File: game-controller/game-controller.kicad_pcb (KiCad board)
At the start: 2 copper layers, 3 parts, among them U1 STM32F103C8T6

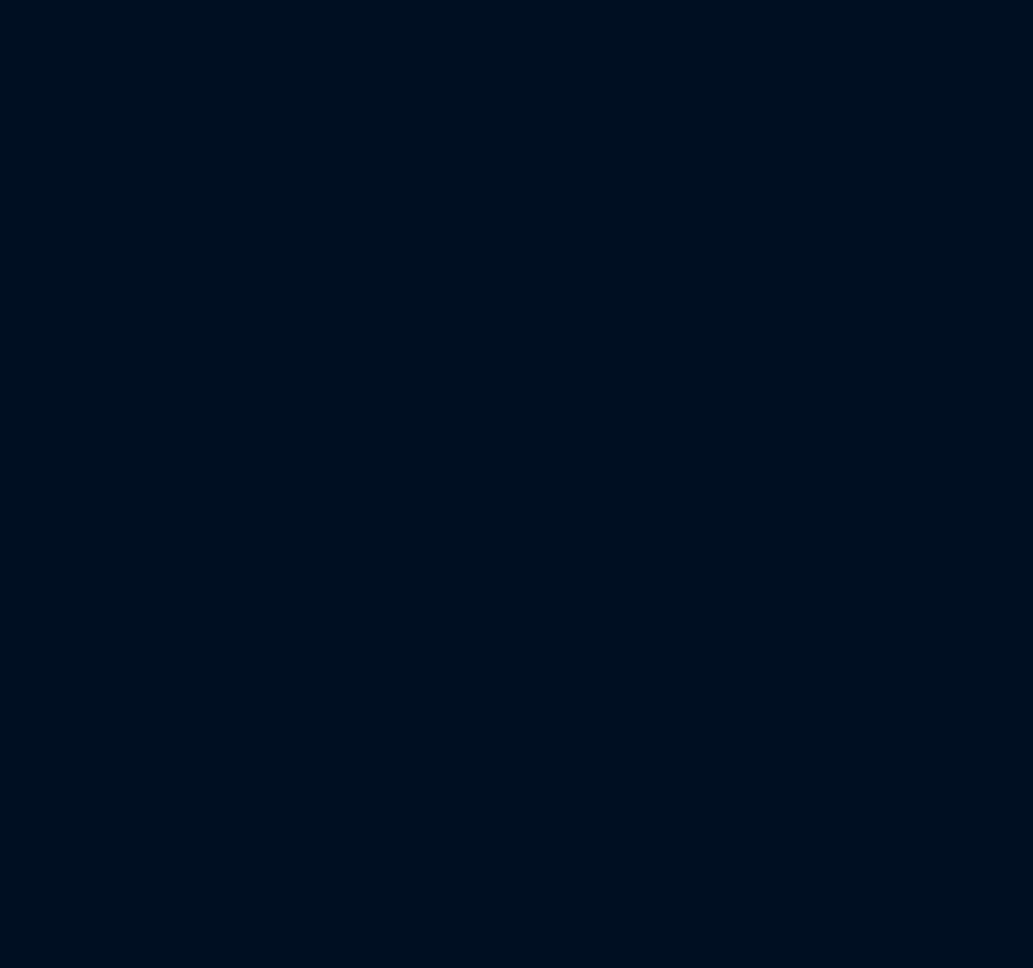
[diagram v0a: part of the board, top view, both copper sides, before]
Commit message: Added footprints
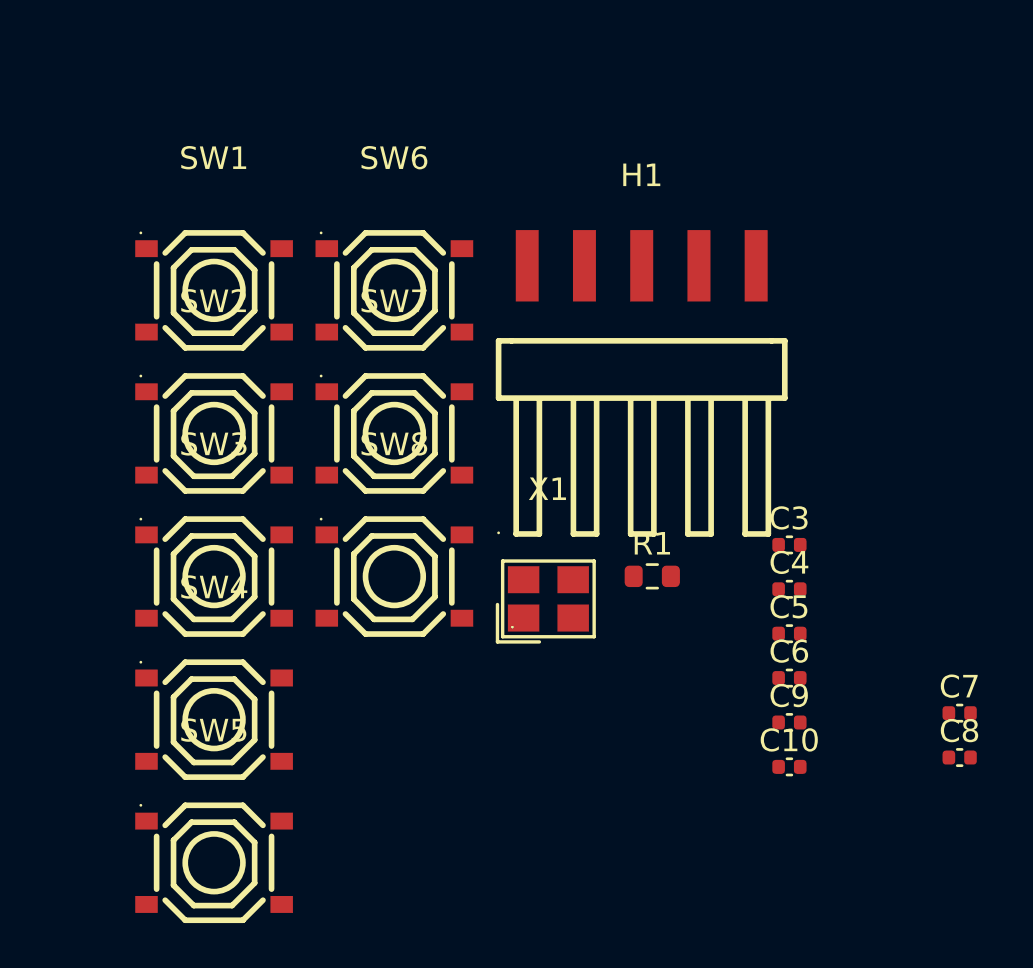
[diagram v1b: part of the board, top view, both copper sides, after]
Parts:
- added C10: 100nF/16V, Capacitor_SMD:C_0402_1005Metric, F.Cu at (208.9, 102.0)
- added C3: 100nF/16V, Capacitor_SMD:C_0402_1005Metric, F.Cu at (208.9, 92.1)
- added C4: 100nF/16V, Capacitor_SMD:C_0402_1005Metric, F.Cu at (208.9, 94.1)
- added C5: 10nF/50V, Capacitor_SMD:C_0402_1005Metric, F.Cu at (208.9, 96.1)
- added C6: 1uF/10V, Capacitor_SMD:C_0402_1005Metric, F.Cu at (208.9, 98.0)
- added C7: 20pF, Capacitor_SMD:C_0402_1005Metric, F.Cu at (216.4, 99.6)
- added C8: 20pF, Capacitor_SMD:C_0402_1005Metric, F.Cu at (216.4, 101.6)
- added C9: 100nF/16V, Capacitor_SMD:C_0402_1005Metric, F.Cu at (208.9, 100.0)
- added H1: HX PZ2.54-1X5P WT, parts:HDR-SMD_5P-P2.54-H-M-W12.8-N, F.Cu at (202.3, 79.8)
- added R1: 1.5kR, Resistor_SMD:R_0603_1608Metric, F.Cu at (202.8, 93.5)
- added SW1: TS-1187A-B-A-B, parts:SW-SMD_4P-L5.1-W5.1-P3.70-LS6.5-TL_H1.5, F.Cu at (183.3, 80.8)
- added SW2: TS-1187A-B-A-B, parts:SW-SMD_4P-L5.1-W5.1-P3.70-LS6.5-TL_H1.5, F.Cu at (183.3, 87.2)
- added SW3: TS-1187A-B-A-B, parts:SW-SMD_4P-L5.1-W5.1-P3.70-LS6.5-TL_H1.5, F.Cu at (183.3, 93.5)
- added SW4: TS-1187A-B-A-B, parts:SW-SMD_4P-L5.1-W5.1-P3.70-LS6.5-TL_H1.5, F.Cu at (183.3, 99.9)
- added SW5: TS-1187A-B-A-B, parts:SW-SMD_4P-L5.1-W5.1-P3.70-LS6.5-TL_H1.5, F.Cu at (183.3, 106.2)
- added SW6: TS-1187A-B-A-B, parts:SW-SMD_4P-L5.1-W5.1-P3.70-LS6.5-TL_H1.5, F.Cu at (191.3, 80.8)
- added SW7: TS-1187A-B-A-B, parts:SW-SMD_4P-L5.1-W5.1-P3.70-LS6.5-TL_H1.5, F.Cu at (191.3, 87.2)
- added SW8: TS-1187A-B-A-B, parts:SW-SMD_4P-L5.1-W5.1-P3.70-LS6.5-TL_H1.5, F.Cu at (191.3, 93.5)
- added X1: TAXM8M4RDBCCT2T, parts:CRYSTAL-SMD_4P-L3.2-W2.5-BL, F.Cu at (198.2, 94.5)
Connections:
- FPC1 pad 1: unconnected-(FPC1-VCC-Pad1) -> +3.3V
- FPC1 pad 2: unconnected-(FPC1-U/D-Pad2) -> /Y-1
- FPC1 pad 3: unconnected-(FPC1-BTN-Pad3) -> /BTN1
- FPC1 pad 4: unconnected-(FPC1-GND-Pad4) -> GND
- FPC1 pad 5: unconnected-(FPC1-L/R-Pad5) -> /X-1
- FPC2 pad 1: unconnected-(FPC2-VCC-Pad1) -> +3.3V
- FPC2 pad 2: unconnected-(FPC2-U/D-Pad2) -> /Y-2
- FPC2 pad 3: unconnected-(FPC2-BTN-Pad3) -> /BTN2
- FPC2 pad 4: unconnected-(FPC2-GND-Pad4) -> GND
- FPC2 pad 5: unconnected-(FPC2-L/R-Pad5) -> /X-2
- U1 pad 1: unconnected-(U1-VBAT-Pad1) -> +3.3V
- U1 pad 11: unconnected-(U1-PA1-Pad11) -> /Y-1
- U1 pad 12: unconnected-(U1-PA2-Pad12) -> /X-1
- U1 pad 13: unconnected-(U1-PA3-Pad13) -> /Y-2
- U1 pad 14: unconnected-(U1-PA4-Pad14) -> /X-2
- U1 pad 16: unconnected-(U1-PA6-Pad16) -> /BTN1
- U1 pad 17: unconnected-(U1-PA7-Pad17) -> /BTN2
- U1 pad 19: unconnected-(U1-PB1-Pad19) -> /DPAD_U
- U1 pad 20: unconnected-(U1-PB2-Pad20) -> /DPAD_L
- U1 pad 21: unconnected-(U1-PB10-Pad21) -> /DPAD_R
- U1 pad 22: unconnected-(U1-PB11-Pad22) -> /DPAD_D
- U1 pad 23: unconnected-(U1-VSS_1-Pad23) -> GND
- U1 pad 24: unconnected-(U1-VDD_1-Pad24) -> +3.3V
- U1 pad 25: unconnected-(U1-PB12-Pad25) -> /A_BTN
- U1 pad 26: unconnected-(U1-PB13-Pad26) -> /B_BTN
- U1 pad 27: unconnected-(U1-PB14-Pad27) -> /X_BTN
- U1 pad 28: unconnected-(U1-PB15-Pad28) -> /Y_BTN
- U1 pad 32: unconnected-(U1-PA11-Pad32) -> /USB_DM
- U1 pad 33: unconnected-(U1-PA12-Pad33) -> /USB_DP
- U1 pad 34: unconnected-(U1-PA13-Pad34) -> /SWDIO
- U1 pad 35: unconnected-(U1-VSS_2-Pad35) -> GND
- U1 pad 36: unconnected-(U1-VDD_2-Pad36) -> +3.3V
- U1 pad 37: unconnected-(U1-PA14-Pad37) -> /SWCLK
- U1 pad 44: unconnected-(U1-BOOT0-Pad44) -> GND
- U1 pad 47: unconnected-(U1-VSS_3-Pad47) -> GND
- U1 pad 48: unconnected-(U1-VDD_3-Pad48) -> +3.3V
- U1 pad 5: unconnected-(U1-PD0-OSC_IN-Pad5) -> /OSC_IN
- U1 pad 6: unconnected-(U1-PD1-OSC_OUT-Pad6) -> /OSC_OUT
- U1 pad 7: unconnected-(U1-NRST-Pad7) -> /NRST
- U1 pad 8: unconnected-(U1-VSSA-Pad8) -> GND
- U1 pad 9: unconnected-(U1-VDDA-Pad9) -> +3.3V

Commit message: Schematics pretty solid now, need to check it again later
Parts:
- added C11: 1uF/10V, Capacitor_SMD:C_0402_1005Metric, F.Cu at (114.4, 62.1)
- added C12: 1uF/10V, Capacitor_SMD:C_0402_1005Metric, F.Cu at (114.4, 64.1)
- added C13: 1uF/10V, Capacitor_SMD:C_0402_1005Metric, F.Cu at (201.8, 107.5)
- added C14: 1uF/10V, Capacitor_SMD:C_0402_1005Metric, F.Cu at (201.8, 109.5)
- added C15: 100nF/16V, Capacitor_SMD:C_0402_1005Metric, F.Cu at (201.8, 111.5)
- added R2: 10kR/±1%, Resistor_SMD:R_0402_1005Metric, F.Cu at (201.9, 105.5)
- added TP1: TestPoint, TestPoint:TestPoint_Pad_1.5x1.5mm, F.Cu at (197.6, 111.0)
- added U2: AP2112K-3.3TRG1, parts:SOT-25-5_L2.9-W1.6-P0.95-LS2.8-BL, F.Cu at (110.9, 63.5)
- added U3: YZ103915020T-04025-02, parts:CONN-SMD_YZ103915020T-04025-01, F.Cu at (115.7, 93.6)
- added U4: AP2112K-3.3TRG1, parts:SOT-25-5_L2.9-W1.6-P0.95-LS2.8-BL, F.Cu at (198.4, 106.9)
- added USB1: AF 90° WJDG, parts:USB-A-TH_AF-WJDG, F.Cu at (117.5, 110.3)
- R1: value 1.5kR -> 1.5kR/±1%
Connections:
- C5 pad 2: +3.3V -> +3.3VA
- C6 pad 2: +3.3V -> +3.3VA
- U1 pad 44: GND -> Net-(U1-BOOT0)
- U1 pad 9: +3.3V -> +3.3VA

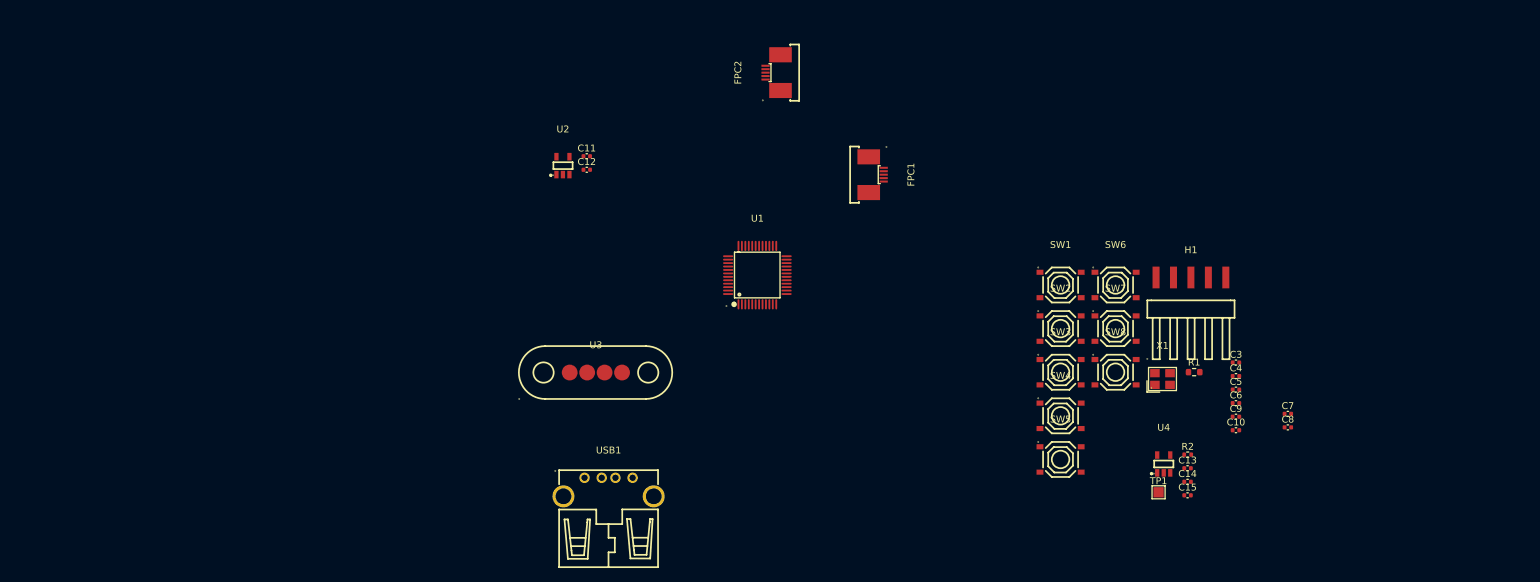
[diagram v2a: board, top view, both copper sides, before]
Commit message: Schematics should be done for front board
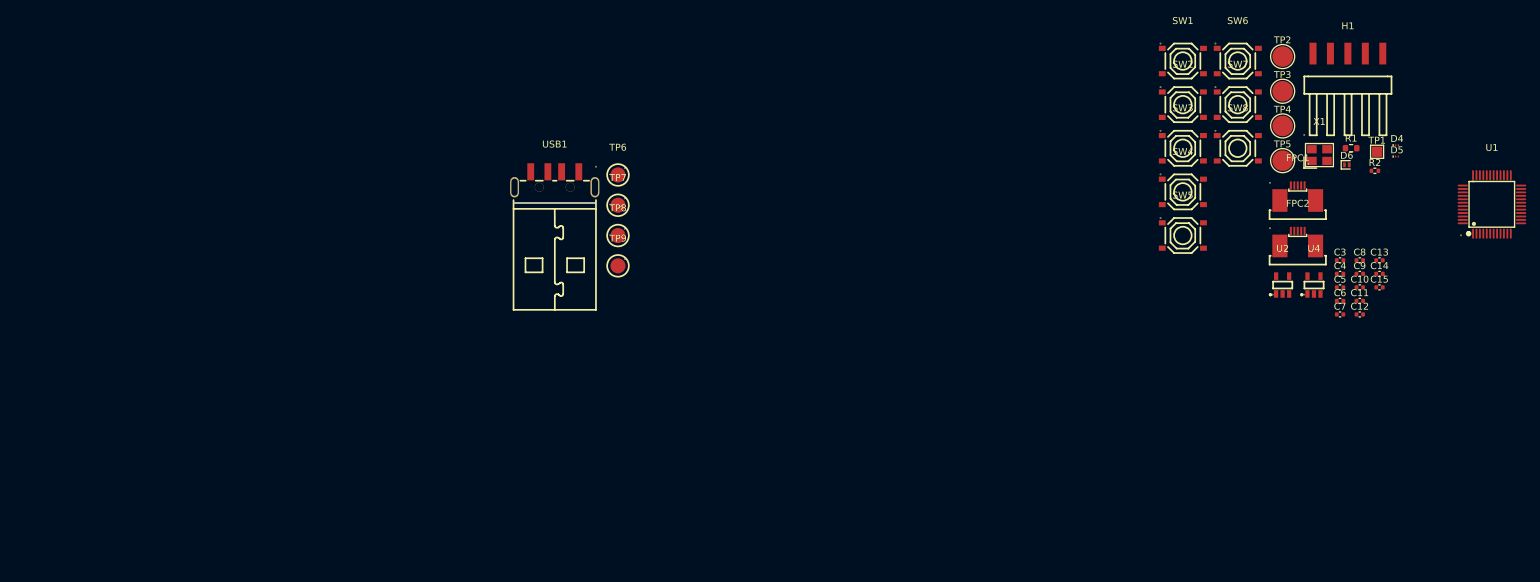
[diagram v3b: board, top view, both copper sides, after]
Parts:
- removed U3: YZ103915020T-04025-02, parts:CONN-SMD_YZ103915020T-04025-01
- added D4: PESD5V0H1BSFYL, Diode_SMD:Nexperia_DSN0603-2_0.6x0.3mm_P0.4mm, F.Cu at (232.3, 60.5)
- added D5: PESD5V0H1BSFYL, Diode_SMD:Nexperia_DSN0603-2_0.6x0.3mm_P0.4mm, F.Cu at (232.3, 62.2)
- added D6: H5VL10B, Diode_SMD:D_SOD-882, F.Cu at (225.0, 63.4)
- added TP2: TestPoint, TestPoint:TestPoint_Pad_D3.0mm, F.Cu at (215.7, 47.6)
- added TP3: TestPoint, TestPoint:TestPoint_Pad_D3.0mm, F.Cu at (215.7, 52.6)
- added TP4: TestPoint, TestPoint:TestPoint_Pad_D3.0mm, F.Cu at (215.7, 57.7)
- added TP5: TestPoint, TestPoint:TestPoint_Pad_D3.0mm, F.Cu at (215.7, 62.7)
- added TP6: BWCD-L3.5W2.0H1.0, parts:SMD_BD2.0-L2.0-W2.0_C9900001905, F.Cu at (118.9, 64.8)
- added TP7: BWCD-L3.5W2.0H1.0, parts:SMD_BD2.0-L2.0-W2.0_C9900001905, F.Cu at (118.9, 69.2)
- added TP8: BWCD-L3.5W2.0H1.0, parts:SMD_BD2.0-L2.0-W2.0_C9900001905, F.Cu at (118.9, 73.7)
- added TP9: BWCD-L3.5W2.0H1.0, parts:SMD_BD2.0-L2.0-W2.0_C9900001905, F.Cu at (118.9, 78.1)
- C4: value 100nF/16V -> 4.7uF/6.3V
- USB1: value AF 90° WJDG -> USB-212-BCW; footprint parts:USB-A-TH_AF-WJDG -> parts:USB-A-SMD_USB-212-BCW
- X1: value TAXM8M4RDBCCT2T -> TAXM8M4RLBDDT2T
- moved C11 114.5 mm to (226.9, 83.2)
- moved C12 114.5 mm to (226.9, 85.1)
- moved U1 107.4 mm to (246.1, 69.1)
- moved U2 106.2 mm to (215.7, 80.9)
- moved FPC2 80.1 mm to (217.9, 74.1), turned to 0 degrees
- moved FPC1 61.4 mm to (217.9, 67.5), turned to 0 degrees
- moved TP1 58.9 mm to (229.4, 61.5)
- moved R2 49.5 mm to (229.1, 64.2)
- moved USB1 45.5 mm to (109.7, 65.5)
- moved C13 41.2 mm to (229.8, 77.3)
- moved C14 41.2 mm to (229.8, 79.2)
- moved C15 41.2 mm to (229.8, 81.2)
- moved H1 39.8 mm to (225.2, 47.2)
- moved R1 39.8 mm to (225.6, 60.9)
- moved X1 39.8 mm to (221.0, 61.9)
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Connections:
- FPC1 pad 1: +3.3V -> +3.3VA
- FPC2 pad 1: +3.3V -> +3.3VA
- USB1 pad 1: +5V -> Net-(USB1-VCC)
- USB1 pad 2: /USB_DM -> Net-(USB1-D-)
- USB1 pad 3: /USB_DP -> Net-(USB1-D+)
- USB1 pad 4: GND -> Net-(USB1-GND)

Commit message: PCB layout in progress...
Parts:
- C10, C11, C12, C13, C14, C15, C3, C4, C5, C6, C7, C8, C9, D4, D5, D6, FPC1, FPC2, R1, R2, TP1, TP2, TP3, TP4, TP5, U1, U2, U4, X1: moved to B.Cu
- moved D4 92.9 mm to (139.9, 70.0), turned to 180 degrees
- moved D5 92.9 mm to (139.9, 71.6), turned to 180 degrees
- moved C13 87.8 mm to (142.5, 86.7), turned to 180 degrees
- moved C14 87.8 mm to (142.5, 88.7), turned to 180 degrees
- moved C15 87.8 mm to (142.5, 90.7), turned to 180 degrees
- moved TP1 87.1 mm to (142.8, 70.9), turned to 180 degrees
- moved R2 86.5 mm to (143.2, 73.7), turned to 180 degrees
- moved U1 83.9 mm to (163.2, 81.9), turned to 180 degrees
- moved C10 82.1 mm to (145.4, 90.7), turned to 180 degrees
- moved C11 82.1 mm to (145.4, 92.6), turned to 180 degrees
- moved C12 82.1 mm to (145.4, 94.6), turned to 180 degrees
- moved C8 82.1 mm to (145.4, 86.7), turned to 180 degrees
- moved C9 82.1 mm to (145.4, 88.7), turned to 180 degrees
- moved R1 79.6 mm to (146.6, 70.4), turned to 180 degrees
- moved D6 78.3 mm to (147.3, 72.8), turned to 180 degrees
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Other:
- board text added: "AntsPCB"
